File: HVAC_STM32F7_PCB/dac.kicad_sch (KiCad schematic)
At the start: 46 parts, among them J10 OUT_Signal_connector, J11 OUT_Signal_connector, J12 OUT_Signal_connector, J13 OUT_Signal_connector, J6 OUT_Signal_connector, J7 OUT_Signal_connector, J8 OUT_Signal_connector, J9 OUT_Signal_connector, U3 DAC7568IAPW, U5 TLV9304xPW, U6 TLV9304xPW

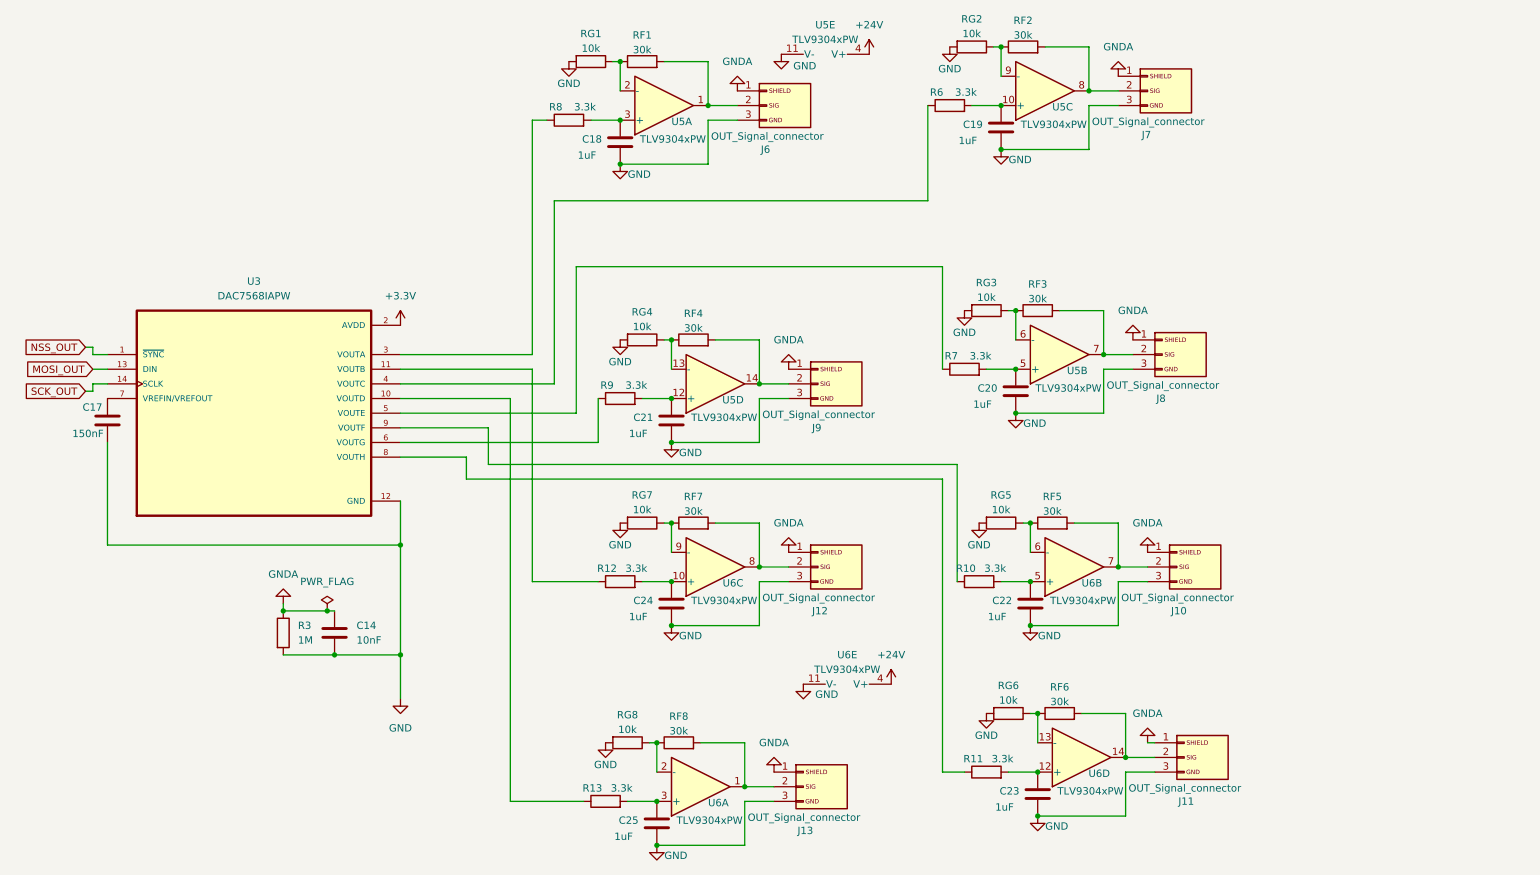
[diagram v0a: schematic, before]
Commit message: ADD Poprawki PCB layout TODO zasilanie toru wyjciowego, podpisy elementow i kosmetyka
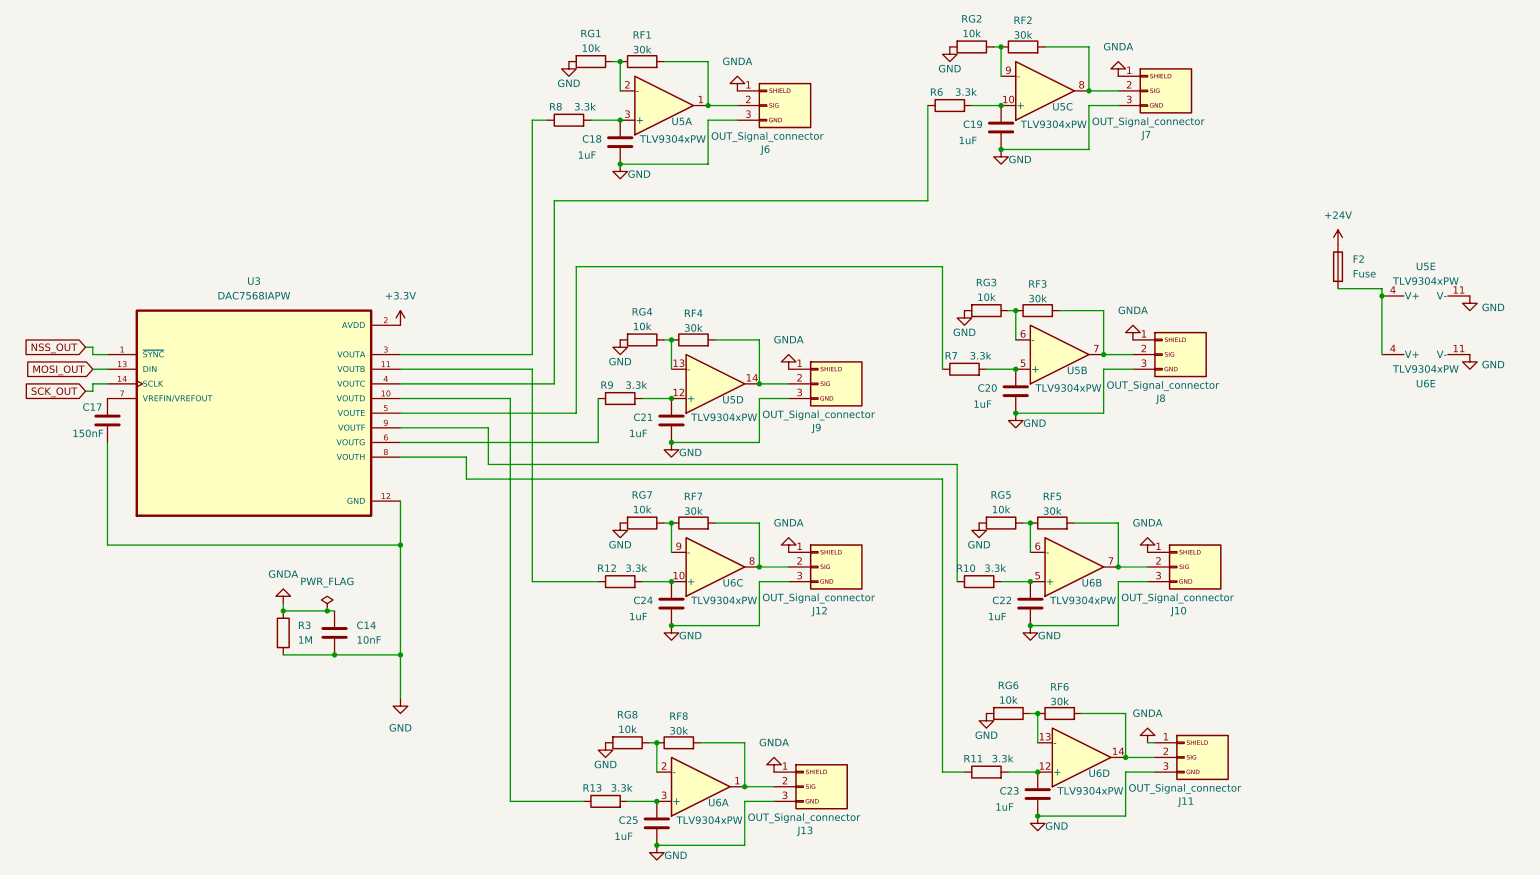
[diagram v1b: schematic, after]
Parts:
- added F2: Fuse, Fuse:Fuse_1812_4532Metric_Pad1.30x3.40mm_HandSolder, symbol Device:Fuse
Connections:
- net +24V: now also F2.1; no longer U5.4 (V+), U6.4 (V+)
- new net: F2.2, U5.4 (V+), U6.4 (V+)
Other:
- moved on the sheet: U5E, U6E
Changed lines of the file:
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@@
 	)
 	(junction
+		(at 248.92 66.04)
+		(diameter 0)
+		(color 0 0 0 0)
+	)
+	(junction
 		(at 132.08 33.02)
 		(diameter 0)
@@
 	(wire
 		(pts
+			(xy 241.3 64.77) (xy 248.92 64.77)
+		)
+		(stroke
+			(width 0)
+			(type default)
+		)
+	)
+	(wire
+		(pts
 			(xy 123.19 148.59) (xy 123.19 143.51)
 		)
@@
 	(wire
 		(pts
+			(xy 248.92 66.04) (xy 248.92 76.2)
+		)
+		(stroke
+			(width 0)
+			(type default)
+		)
+	)
+	(wire
+		(pts
 			(xy 113.03 91.44) (xy 113.03 83.82)
 		)
@@
 	(wire
 		(pts
+			(xy 248.92 64.77) (xy 248.92 66.04)
+		)
+		(stroke
+			(width 0)
+			(type default)
+		)
+	)
+	(wire
+		(pts
 			(xy 200.66 76.2) (xy 205.74 76.2)
 		)
@@
 	)
 	(symbol
+		(lib_id "Device:Fuse")
+		(at 241.3 60.96 0)
+		(unit 1)
+		(exclude_from_sim no)
+		(in_bom yes)
+		(on_board yes)
+		(dnp no)
+		(fields_autoplaced yes)
+		(property "Reference" "F2"
+			(at 243.84 59.6899 0)
+			(effects
+				(font
+					(size 1.27 1.27)
+				)
+				(justify left)
+			)
+		)
+		(property "Value" "Fuse"
+			(at 243.84 62.2299 0)
+			(effects
+				(font
+					(size 1.27 1.27)
+				)
+				(justify left)
+			)
+		)
+		(property "Footprint" "Fuse:Fuse_1812_4532Metric_Pad1.30x3.40mm_HandSolder"
+			(at 239.522 60.96 90)
+			(effects
+				(font
+					(size 1.27 1.27)
+				)
+				(hide yes)
+			)
+		)
+		(property "Datasheet" "~"
+			(at 241.3 60.96 0)
+			(effects
+				(font
+					(size 1.27 1.27)
+				)
+				(hide yes)
+			)
+		)
+		(property "Description" "Fuse"
+			(at 241.3 60.96 0)
+			(effects
+				(font
+					(size 1.27 1.27)
+				)
+				(hide yes)
+			)
+		)
+		(pin "1"
+		)
+		(pin "2"
+		)
+		(instances
+			(project ""
+				(path "/79f65717-d4aa-4d9b-9389-67dd3cbc0c4f/85080b76-4579-4719-938b-0be3843c3f61"
+					(reference "F2")
+					(unit 1)
+				)
+			)
+		)
+	)
+	(symbol
 		(lib_id "Device:R")
 		(at 189.23 68.58 90)
@@
 	(symbol
 		(lib_id "power:GND")
-		(at 144.78 24.13 0)
+		(at 264.16 66.04 0)
 		(unit 1)
 		(exclude_from_sim no)
@@
 		(dnp no)
 		(property "Reference" "#PWR034"
-			(at 144.78 30.48 0)
+			(at 264.16 72.39 0)
 			(effects
 				(font
@@
 		)
 		(property "Value" "GND"
-			(at 148.844 26.162 0)
+			(at 268.224 68.072 0)
 			(effects
 				(font
@@
 		)
 		(property "Footprint" ""
-			(at 144.78 24.13 0)
+			(at 264.16 66.04 0)
 			(effects
 				(font
@@
 		)
 		(property "Datasheet" ""
-			(at 144.78 24.13 0)
+			(at 264.16 66.04 0)
 			(effects
 				(font
@@
 		)
 		(property "Description" "Power symbol creates a global label with name \"GND\" , ground"
-			(at 144.78 24.13 0)
+			(at 264.16 66.04 0)
 			(effects
 				(font
@@
 	(symbol
 		(lib_id "Amplifier_Operational:TLV9304xPW")
-		(at 156.21 130.81 270)
+		(at 256.54 78.74 90)
 		(mirror x)
 		(unit 5)
@@
 		(fields_autoplaced yes)
 		(property "Reference" "U6"
-			(at 156.21 128.27 90)
+			(at 256.54 81.28 90)
 			(effects
 				(font
@@
 		)
 		(property "Value" "TLV9304xPW"
-			(at 156.21 130.81 90)
+			(at 256.54 78.74 90)
 			(effects
 				(font
@@
 		)
 		(property "Footprint" "Package_SO:TSSOP-14_4.4x5mm_P0.65mm"
-			(at 158.75 132.08 0)
+			(at 254 77.47 0)
 			(effects
 				(font
@@
 		)
 		(property "Datasheet" "https://www.ti.com/lit/ds/symlink/tlv9304.pdf"
-			(at 161.29 129.54 0)
+			(at 251.46 80.01 0)
 			(effects
 				(font
@@
 		)
 		(property "Description" "40-V, 1-MHz, RRO Operational Amplifiers for Cost-Sensitive Systems, TSSOP-14"
-			(at 156.21 130.81 0)
+			(at 256.54 78.74 0)
 			(effects
 				(font
@@
 	)
 	(symbol
-		(lib_id "power:+24V")
-		(at 160.02 24.13 0)
-		(unit 1)
-		(exclude_from_sim no)
-		(in_bom yes)
-		(on_board yes)
-		(dnp no)
-		(fields_autoplaced yes)
-		(property "Reference" "#PWR037"
-			(at 160.02 27.94 0)
-			(effects
-				(font
-					(size 1.27 1.27)
-				)
-				(hide yes)
-			)
-		)
-		(property "Value" "+24V"
-			(at 160.02 19.05 0)
-			(effects
-				(font
-					(size 1.27 1.27)
-				)
-			)
-		)
-		(property "Footprint" ""
-			(at 160.02 24.13 0)
-			(effects
-				(font
-					(size 1.27 1.27)
-				)
-				(hide yes)
-			)
-		)
-		(property "Datasheet" ""
-			(at 160.02 24.13 0)
-			(effects
-				(font
-					(size 1.27 1.27)
-				)
-				(hide yes)
-			)
-		)
-		(property "Description" "Power symbol creates a global label with name \"+24V\""
-			(at 160.02 24.13 0)
-			(effects
-				(font
-					(size 1.27 1.27)
-				)
-				(hide yes)
-			)
-		)
-		(pin "1"
-		)
-		(instances
-			(project ""
-				(path "/79f65717-d4aa-4d9b-9389-67dd3cbc0c4f/85080b76-4579-4719-938b-0be3843c3f61"
-					(reference "#PWR037")
-					(unit 1)
-				)
-			)
-		)
-	)
-	(symbol
 		(lib_id "power:GNDA")
 		(at 146.05 78.74 180)
@@
 	(symbol
 		(lib_id "Amplifier_Operational:TLV9304xPW")
-		(at 152.4 21.59 270)
+		(at 256.54 68.58 90)
 		(mirror x)
 		(unit 5)
@@
 		(fields_autoplaced yes)
 		(property "Reference" "U5"
-			(at 152.4 19.05 90)
+			(at 256.54 60.96 90)
 			(effects
 				(font
@@
 		)
 		(property "Value" "TLV9304xPW"
-			(at 152.4 21.59 90)
+			(at 256.54 63.5 90)
 			(effects
 				(font
@@
 		)
 		(property "Footprint" "Package_SO:TSSOP-14_4.4x5mm_P0.65mm"
-			(at 154.94 22.86 0)
+			(at 254 67.31 0)
 			(effects
 				(font
@@
 		)
 		(property "Datasheet" "https://www.ti.com/lit/ds/symlink/tlv9304.pdf"
-			(at 157.48 20.32 0)
+			(at 251.46 69.85 0)
 			(effects
 				(font
@@
 		)
 		(property "Description" "40-V, 1-MHz, RRO Operational Amplifiers for Cost-Sensitive Systems, TSSOP-14"
-			(at 152.4 21.59 0)
+			(at 256.54 68.58 0)
 			(effects
 				(font
@@
 	(symbol
 		(lib_id "power:+24V")
-		(at 163.83 133.35 0)
+		(at 241.3 57.15 0)
 		(unit 1)
 		(exclude_from_sim no)
@@
 		(dnp no)
 		(fields_autoplaced yes)
-		(property "Reference" "#PWR033"
-			(at 163.83 137.16 0)
+		(property "Reference" "#PWR037"
+			(at 241.3 60.96 0)
 			(effects
 				(font
@@
 		)
 		(property "Value" "+24V"
-			(at 163.83 128.27 0)
+			(at 241.3 52.07 0)
 			(effects
 				(font
@@
 		)
 		(property "Footprint" ""
-			(at 163.83 133.35 0)
+			(at 241.3 57.15 0)
 			(effects
 				(font
@@
 		)
 		(property "Datasheet" ""
-			(at 163.83 133.35 0)
+			(at 241.3 57.15 0)
 			(effects
 				(font
@@
 		)
 		(property "Description" "Power symbol creates a global label with name \"+24V\""
-			(at 163.83 133.35 0)
+			(at 241.3 57.15 0)
 			(effects
 				(font
@@
 		)
 		(instances
-			(project "HVAC_STM32F7_PCB"
+			(project ""
 				(path "/79f65717-d4aa-4d9b-9389-67dd3cbc0c4f/85080b76-4579-4719-938b-0be3843c3f61"
-					(reference "#PWR033")
+					(reference "#PWR037")
 					(unit 1)
 				)
@@
 	(symbol
 		(lib_id "power:GND")
-		(at 148.59 133.35 0)
+		(at 264.16 76.2 0)
 		(unit 1)
 		(exclude_from_sim no)
@@
 		(dnp no)
 		(property "Reference" "#PWR035"
-			(at 148.59 139.7 0)
+			(at 264.16 82.55 0)
 			(effects
 				(font
@@
 		)
 		(property "Value" "GND"
-			(at 152.654 135.128 0)
+			(at 268.224 77.978 0)
 			(effects
 				(font
@@
 		)
 		(property "Footprint" ""
-			(at 148.59 133.35 0)
+			(at 264.16 76.2 0)
 			(effects
 				(font
@@
 		)
 		(property "Datasheet" ""
-			(at 148.59 133.35 0)
+			(at 264.16 76.2 0)
 			(effects
 				(font
@@
 		)
 		(property "Description" "Power symbol creates a global label with name \"GND\" , ground"
-			(at 148.59 133.35 0)
+			(at 264.16 76.2 0)
 			(effects
 				(font

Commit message: ADD final pcb version for review, god bless
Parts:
- added C28, C32, C33: 100n, Capacitor_SMD:C_0805_2012Metric_Pad1.18x1.45mm_HandSolder, symbol Device:C
- added C29: 4.7u/50V, Capacitor_SMD:C_2220_5750Metric_Pad1.97x5.40mm_HandSolder, symbol Device:C_Polarized
- added C30: 10u, Capacitor_SMD:C_0805_2012Metric_Pad1.18x1.45mm_HandSolder, symbol Device:C
- added C31: 100n/50V, Capacitor_SMD:C_0805_2012Metric_Pad1.18x1.45mm_HandSolder, symbol Device:C_Polarized
- added R17: 10k, Resistor_SMD:R_0805_2012Metric_Pad1.20x1.40mm_HandSolder, symbol Device:R
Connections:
- net +24V: now also F2.2; no longer F2.1
- net GND: now also C28.2, C29.2, C30.2, C31.2, C32.2, C33.2
- net at U5.4 (V+), U6.4 (V+): now also C30.1, C31.1, C32.1, C33.1, R17.1; no longer F2.2
- new net: C28.1, C29.1, F2.1, R17.2
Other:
- moved on the sheet: F2, U5E, U6E

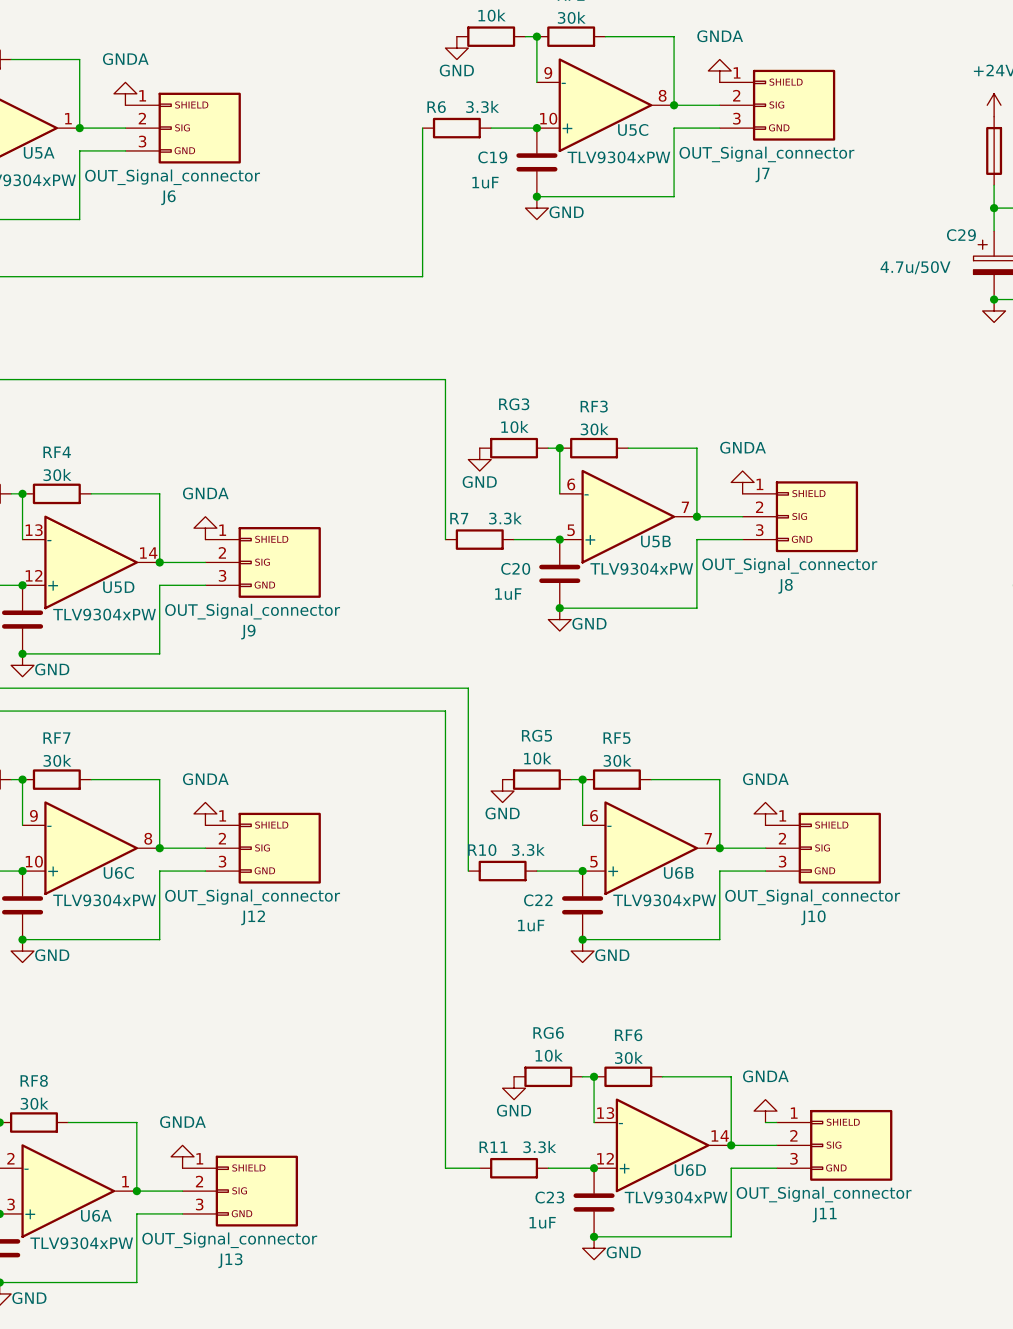
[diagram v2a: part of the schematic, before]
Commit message: ADD: opis części hardware, dodane zdjęcia i schematy
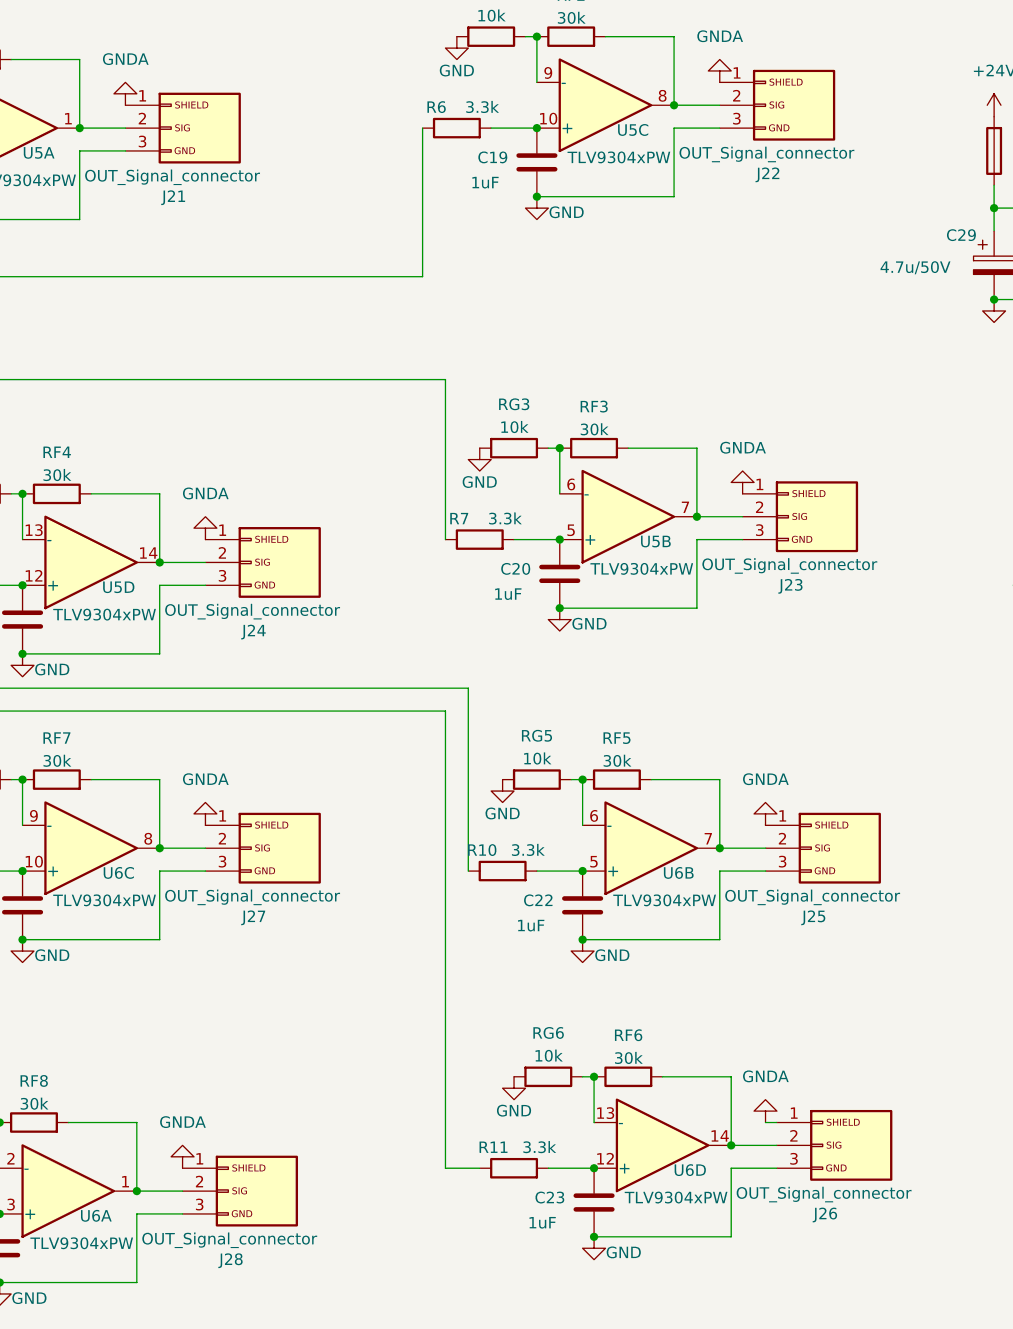
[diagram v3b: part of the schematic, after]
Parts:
- renumbered J6 to J21, J7 to J22, J8 to J23, J9 to J24, J10 to J25, J11 to J26, J12 to J27, J13 to J28
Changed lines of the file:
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@@
 		(on_board yes)
 		(dnp no)
-		(property "Reference" "J8"
+		(property "Reference" "J23"
 			(at 209.804 83.82 0)
 			(effects
@@
 			(project "test_project"
 				(path "/79f65717-d4aa-4d9b-9389-67dd3cbc0c4f/85080b76-4579-4719-938b-0be3843c3f61"
-					(reference "J8")
+					(reference "J23")
 					(unit 1)
 				)
@@
 		(on_board yes)
 		(dnp no)
-		(property "Reference" "J13"
+		(property "Reference" "J28"
 			(at 147.574 158.75 0)
 			(effects
@@
 			(project "test_project"
 				(path "/79f65717-d4aa-4d9b-9389-67dd3cbc0c4f/85080b76-4579-4719-938b-0be3843c3f61"
-					(reference "J13")
+					(reference "J28")
 					(unit 1)
 				)
@@
 		(on_board yes)
 		(dnp no)
-		(property "Reference" "J9"
+		(property "Reference" "J24"
 			(at 150.114 88.9 0)
 			(effects
@@
 			(project "test_project"
 				(path "/79f65717-d4aa-4d9b-9389-67dd3cbc0c4f/85080b76-4579-4719-938b-0be3843c3f61"
-					(reference "J9")
+					(reference "J24")
 					(unit 1)
 				)
@@
 		(on_board yes)
 		(dnp no)
-		(property "Reference" "J6"
+		(property "Reference" "J21"
 			(at 141.224 40.64 0)
 			(effects
@@
 			(project "test_project"
 				(path "/79f65717-d4aa-4d9b-9389-67dd3cbc0c4f/85080b76-4579-4719-938b-0be3843c3f61"
-					(reference "J6")
+					(reference "J21")
 					(unit 1)
 				)
@@
 		(on_board yes)
 		(dnp no)
-		(property "Reference" "J10"
+		(property "Reference" "J25"
 			(at 212.344 120.65 0)
 			(effects
@@
 			(project "test_project"
 				(path "/79f65717-d4aa-4d9b-9389-67dd3cbc0c4f/85080b76-4579-4719-938b-0be3843c3f61"
-					(reference "J10")
+					(reference "J25")
 					(unit 1)
 				)
@@
 		(on_board yes)
 		(dnp no)
-		(property "Reference" "J7"
+		(property "Reference" "J22"
 			(at 207.264 38.1 0)
 			(effects
@@
 			(project "test_project"
 				(path "/79f65717-d4aa-4d9b-9389-67dd3cbc0c4f/85080b76-4579-4719-938b-0be3843c3f61"
-					(reference "J7")
+					(reference "J22")
 					(unit 1)
 				)
@@
 		(on_board yes)
 		(dnp no)
-		(property "Reference" "J12"
+		(property "Reference" "J27"
 			(at 150.114 120.65 0)
 			(effects
@@
 			(project "test_project"
 				(path "/79f65717-d4aa-4d9b-9389-67dd3cbc0c4f/85080b76-4579-4719-938b-0be3843c3f61"
-					(reference "J12")
+					(reference "J27")
 					(unit 1)
 				)
@@
 		(on_board yes)
 		(dnp no)
-		(property "Reference" "J11"
+		(property "Reference" "J26"
 			(at 213.614 153.67 0)
 			(effects
@@
 			(project "test_project"
 				(path "/79f65717-d4aa-4d9b-9389-67dd3cbc0c4f/85080b76-4579-4719-938b-0be3843c3f61"
-					(reference "J11")
+					(reference "J26")
 					(unit 1)
 				)
